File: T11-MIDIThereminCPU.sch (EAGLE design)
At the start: 66 parts, among them IC1 UA78M05DCY, IC4 QUAD_OPAMPD, IC5 4069D, J1 DCJ0202, Q1 16MHz, U1 ATMEGA328P-AU

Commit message: Add files via upload
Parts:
- removed C14: 0.1u, adafruit:C-USC0805
- removed C9: 100n, adafruit:C-USC0805
- removed IC4: QUAD_OPAMPD, adafruit:QUAD_OPAMPD
- removed JP3: (no value), adafruit:PINHD-1X12
- removed R18, R19, R20: 10k, pot:TRIM_US-B25U
- removed R21, R22, R23: 1k, resistor:R-US_R0805
- removed U$3, U$4: 1k@100MHz, adafruit:FB
- added JP4: (no value), adafruit:PINHD-1X6
- C10: value 0.1u -> 100uF; device adafruit:C-USC0805 -> adafruit:CPOL-USE3.5-8
- C7, C8: value 100n -> 100uF; device adafruit:C-USC0805 -> adafruit:CPOL-USE3.5-8
- D1, D4, D5: device diode:ZENER-DIODEDO35Z10 -> diode:1N4148DO35-7
- D2, D3: value 1N4004 -> 1N4148DO35-7; device diode:1N4004 -> diode:1N4148DO35-7
- R10, R8, R9: value 1k -> 100
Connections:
- removed net N$1: U$2G$1.4, U$4.1
- removed net N$18: IC4C.-IN, R20.S, R23.2
- removed net N$19: IC4A.-IN, R18.S, R21.1
- removed net N$21: D1.C, R23.1, U$1G$1.1
- removed net N$22: IC4B.-IN, R19.S, R22.2
- removed net N$23: D4.C, R21.2, U$6G$1.1
- removed net N$25: D5.C, R22.1, U$5G$1.1
- removed net N$3: U$2G$1.5, U$3.2
- net +12V: no longer C10.1, C14.1, IC4P.V+, JP3.1
- net +5V: no longer JP3.2
- net ANALOG_IN_1: now also D1.C, JP4.1, U$1G$1.1; no longer IC4C.OUT, JP3.5, R20.A
- net ANALOG_IN_2: now also D5.C, JP4.2, U$5G$1.1; no longer IC4B.OUT, JP3.6, R19.A
- net ANALOG_IN_3: now also D4.C, JP4.3, U$6G$1.1; no longer IC4A.OUT, JP3.7, R18.A
- net GND: now also C10.-, C7.-, C8.-, IC5B.I; no longer C10.2, C14.2, C7.1, C8.1, C9.1, IC4A.+IN, IC4B.+IN, IC4C.+IN, IC4D.+IN, IC4D.-IN, IC4P.V-, IC5F.I, JP3.3
- net INT0: now also IC5A.O; no longer IC5B.O, JP3.11
- net INT1: now also IC5F.O; no longer IC5A.O, JP3.12
- net MOSI: now also JP4.6; no longer JP3.10
- net N$10: now also C10.+; no longer C8.2
- net N$13: now also U$2G$1.5; no longer U$3.1
- net N$14: now also IC5A.I; no longer IC5B.I
- net N$2: now also U$2G$1.4; no longer U$4.2
- net N$26: now also C7.+; no longer C7.2
- net N$5: now also C8.+; no longer C9.2
- net N$6: now also IC5F.I; no longer IC5A.I
- net PC3: now also JP2.3; no longer JP2.1
- net PC5: now also JP2.1; no longer JP2.3
- net SIGNAL_OUT_1: now also JP4.4; no longer JP3.8
- net SIGNAL_OUT_2: now also JP4.5; no longer JP3.9
- net TX: no longer JP3.4
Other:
- note added: "MIDI OUTPUT"
- note added: "SENSOR CONNECTOR 1"
- note added: "SENSOR CONNECTOR 2"
- note added: "SENSOR CONNECTOR 3"
- note added: "User Select and Calibration Buttons"
- note removed: "Input buttons"
- note removed: "LED Indicators"
- note removed: "NC Op-Amp"
- note removed: "Output"
- note removed: "To Sensor Board"
- moved on the sheet: C1, C11, C12, C13, C15, C2, C3, C4, C5, C6, IC1, IC5A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

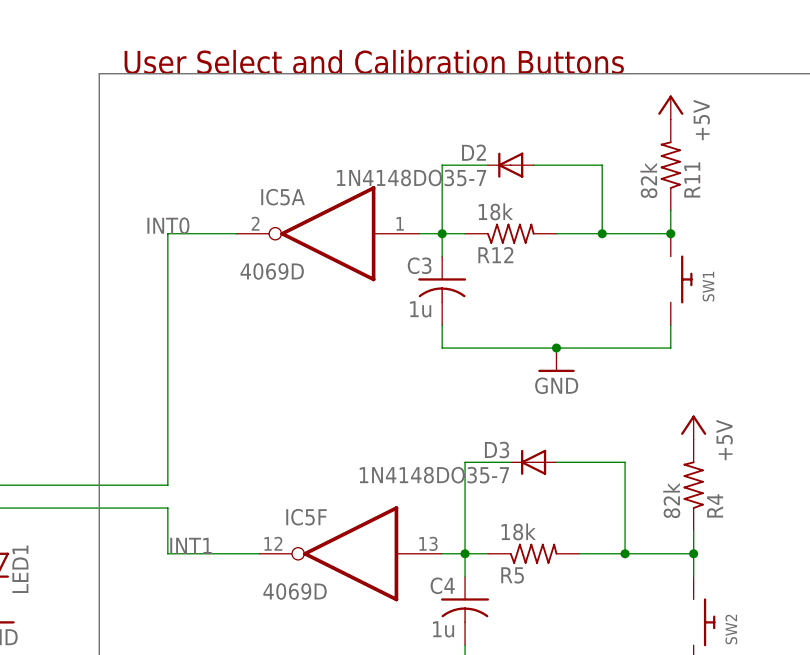
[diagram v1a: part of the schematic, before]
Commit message: Created BOM, updated parts
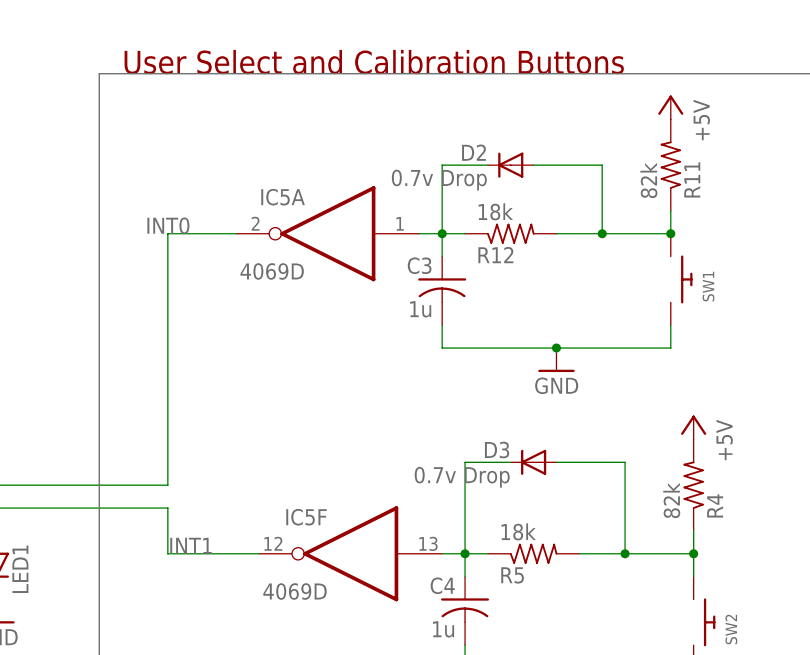
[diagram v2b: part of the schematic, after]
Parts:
- D2, D3: value 1N4148DO35-7 -> 0.7v Drop
- IC1: DIGIKEYNUMBER (none) -> 296-12290-1-ND; PARTNUMBER (none) -> UA78M05CDCYR
- IC5: DIGIKEYNUMBER (none) -> 296-28484-1-ND; PARTNUMBER (none) -> SN7414DR
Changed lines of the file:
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@@
 <?xml version="1.0" encoding="utf-8"?>
 <!DOCTYPE eagle SYSTEM "eagle.dtd">
-<eagle version="7.7.0">
+<eagle version="7.6.0">
 <drawing>
 <settings>
@@
 <setting verticaltext="up"/>
 </settings>
-<grid distance="0.05" unitdist="inch" unit="inch" style="lines" multiple="2" display="no" altdistance="0.01" altunitdist="inch" altunit="inch"/>
+<grid distance="0.1" unitdist="inch" unit="inch" style="lines" multiple="1" display="no" altdistance="0.01" altunitdist="inch" altunit="inch"/>
 <layers>
-<layer number="1" name="Top" color="4" fill="1" visible="no" active="no"/>
-<layer number="16" name="Bottom" color="1" fill="1" visible="no" active="no"/>
-<layer number="17" name="Pads" color="2" fill="1" visible="no" active="no"/>
-<layer number="18" name="Vias" color="2" fill="1" visible="no" active="no"/>
-<layer number="19" name="Unrouted" color="6" fill="1" visible="no" active="no"/>
-<layer number="20" name="Dimension" color="15" fill="1" visible="no" active="no"/>
-<layer number="21" name="tPlace" color="7" fill="1" visible="no" active="no"/>
-<layer number="22" name="bPlace" color="7" fill="1" visible="no" active="no"/>
-<layer number="23" name="tOrigins" color="15" fill="1" visible="no" active="no"/>
-<layer number="24" name="bOrigins" color="15" fill="1" visible="no" active="no"/>
-<layer number="25" name="tNames" color="7" fill="1" visible="no" active="no"/>
-<layer number="26" name="bNames" color="7" fill="1" visible="no" active="no"/>
-<layer number="27" name="tValues" color="7" fill="1" visible="no" active="no"/>
-<layer number="28" name="bValues" color="7" fill="1" visible="no" active="no"/>
+<layer number="1" name="Top" color="4" fill="1" visible="yes" active="no"/>
+<layer number="16" name="Bottom" color="1" fill="1" visible="yes" active="no"/>
+<layer number="17" name="Pads" color="2" fill="1" visible="yes" active="no"/>
+<layer number="18" name="Vias" color="2" fill="1" visible="yes" active="no"/>
+<layer number="19" name="Unrouted" color="6" fill="1" visible="yes" active="no"/>
+<layer number="20" name="Dimension" color="15" fill="1" visible="yes" active="no"/>
+<layer number="21" name="tPlace" color="7" fill="1" visible="yes" active="no"/>
+<layer number="22" name="bPlace" color="7" fill="1" visible="yes" active="no"/>
+<layer number="23" name="tOrigins" color="15" fill="1" visible="yes" active="no"/>
+<layer number="24" name="bOrigins" color="15" fill="1" visible="yes" active="no"/>
+<layer number="25" name="tNames" color="7" fill="1" visible="yes" active="no"/>
+<layer number="26" name="bNames" color="7" fill="1" visible="yes" active="no"/>
+<layer number="27" name="tValues" color="7" fill="1" visible="yes" active="no"/>
+<layer number="28" name="bValues" color="7" fill="1" visible="yes" active="no"/>
 <layer number="29" name="tStop" color="7" fill="3" visible="no" active="no"/>
 <layer number="30" name="bStop" color="7" fill="6" visible="no" active="no"/>
@@
 <layer number="35" name="tGlue" color="7" fill="4" visible="no" active="no"/>
 <layer number="36" name="bGlue" color="7" fill="5" visible="no" active="no"/>
-<layer number="37" name="tTest" color="7" fill="1" visible="no" active="no"/>
-<layer number="38" name="bTest" color="7" fill="1" visible="no" active="no"/>
+<layer number="37" name="tTest" color="7" fill="1" visible="yes" active="no"/>
+<layer number="38" name="bTest" color="7" fill="1" visible="yes" active="no"/>
 <layer number="39" name="tKeepout" color="4" fill="11" visible="no" active="no"/>
 <layer number="40" name="bKeepout" color="1" fill="11" visible="no" active="no"/>
@@
 <layer number="44" name="Drills" color="7" fill="1" visible="no" active="no"/>
 <layer number="45" name="Holes" color="7" fill="1" visible="no" active="no"/>
-<layer number="46" name="Milling" color="3" fill="1" visible="no" active="no"/>
-<layer number="47" name="Measures" color="7" fill="1" visible="no" active="no"/>
-<layer number="48" name="Document" color="7" fill="1" visible="no" active="no"/>
-<layer number="49" name="Reference" color="7" fill="1" visible="no" active="no"/>
-<layer number="50" name="dxf" color="7" fill="1" visible="no" active="no"/>
-<layer number="51" name="tDocu" color="7" fill="1" visible="no" active="no"/>
-<layer number="52" name="bDocu" color="7" fill="1" visible="no" active="no"/>
-<layer number="53" name="tGND_GNDA" color="7" fill="9" visible="no" active="no"/>
-<layer number="54" name="bGND_GNDA" color="1" fill="9" visible="no" active="no"/>
-<layer number="56" name="wert" color="7" fill="1" visible="no" active="no"/>
-<layer number="57" name="tCAD" color="7" fill="1" visible="no" active="no"/>
-<layer number="59" name="tCarbon" color="7" fill="1" visible="no" active="no"/>
-<layer number="60" name="bCarbon" color="7" fill="1" visible="no" active="no"/>
+<layer number="46" name="Milling" color="3" fill="1" visible="yes" active="no"/>
+<layer number="47" name="Measures" color="7" fill="1" visible="yes" active="no"/>
+<layer number="48" name="Document" color="7" fill="1" visible="yes" active="no"/>
+<layer number="49" name="Reference" color="7" fill="1" visible="yes" active="no"/>
+<layer number="50" name="dxf" color="7" fill="1" visible="yes" active="no"/>
+<layer number="51" name="tDocu" color="7" fill="1" visible="yes" active="no"/>
+<layer number="52" name="bDocu" color="7" fill="1" visible="yes" active="no"/>
+<layer number="53" name="tGND_GNDA" color="7" fill="9" visible="yes" active="no"/>
+<layer number="54" name="bGND_GNDA" color="1" fill="9" visible="yes" active="no"/>
+<layer number="56" name="wert" color="7" fill="1" visible="yes" active="no"/>
+<layer number="57" name="tCAD" color="7" fill="1" visible="yes" active="no"/>
+<layer number="59" name="tCarbon" color="7" fill="1" visible="yes" active="no"/>
+<layer number="60" name="bCarbon" color="7" fill="1" visible="yes" active="no"/>
 <layer number="90" name="Modules" color="5" fill="1" visible="yes" active="yes"/>
 <layer number="91" name="Nets" color="2" fill="1" visible="yes" active="yes"/>
@@
 <part name="SUPPLY1" library="supply2" deviceset="GND" device=""/>
 <part name="JP1" library="pinhead" deviceset="PINHD-2X3" device=""/>
-<part name="IC1" library="linear" deviceset="UA78M*" device="DCY" technology="05"/>
+<part name="IC1" library="linear" deviceset="UA78M*" device="DCY" technology="05">
+<attribute name="DIGIKEYNUMBER" value="296-12290-1-ND"/>
+<attribute name="PARTNUMBER" value="UA78M05CDCYR"/>
+</part>
 <part name="J1" library="con-jack" deviceset="DCJ0202" device=""/>
 <part name="C5" library="adafruit" deviceset="C-US" device="C0805" value="0.33u"/>
@@
 <part name="R12" library="resistor" deviceset="R-US_" device="R0805" value="18k"/>
 <part name="C3" library="adafruit" deviceset="C-US" device="C0805" value="1u"/>
-<part name="D2" library="diode" deviceset="1N4148" device="DO35-7"/>
+<part name="D2" library="diode" deviceset="1N4148" device="DO35-7" value="0.7v Drop"/>
 <part name="R4" library="resistor" deviceset="R-US_" device="R0805" value="82k"/>
 <part name="SW2" library="adafruit" deviceset="SWITCH_PUSHBUTTON" device="SOFTTOUCHSMD_SJ"/>
 <part name="R5" library="resistor" deviceset="R-US_" device="R0805" value="18k"/>
-<part name="D3" library="diode" deviceset="1N4148" device="DO35-7"/>
+<part name="D3" library="diode" deviceset="1N4148" device="DO35-7" value="0.7v Drop"/>
 <part name="C4" library="adafruit" deviceset="C-US" device="C0805" value="1u"/>
 <part name="U$5" library="adafruit" deviceset="MIDIJACK" device=""/>
@@
 <part name="GND25" library="supply1" deviceset="GND" device=""/>
 <part name="GND26" library="supply1" deviceset="GND" device=""/>
-<part name="IC5" library="40xx" deviceset="4069" device="D"/>
+<part name="IC5" library="40xx" deviceset="4069" device="D">
+<attribute name="DIGIKEYNUMBER" value="296-28484-1-ND"/>
+<attribute name="PARTNUMBER" value="SN7414DR"/>
+</part>
 <part name="P+5" library="supply1" deviceset="+5V" device=""/>
 <part name="GND5" library="supply1" deviceset="GND" device=""/>
@@
 <instance part="SUPPLY1" gate="GND" x="156.21" y="226.06"/>
 <instance part="JP1" gate="A" x="172.72" y="193.04"/>
-<instance part="IC1" gate="G$1" x="332.74" y="228.6"/>
+<instance part="IC1" gate="G$1" x="332.74" y="228.6">
+<attribute name="DIGIKEYNUMBER" x="332.74" y="228.6" size="1.778" layer="96" display="off"/>
+<attribute name="PARTNUMBER" x="332.74" y="228.6" size="1.778" layer="96" display="off"/>
+</instance>
 <instance part="J1" gate="G$1" x="290.83" y="223.52" rot="MR180"/>
 <instance part="C5" gate="G$1" x="320.04" y="220.98"/>
@@
 <instance part="IC5" gate="B" x="224.79" y="15.24"/>
 <instance part="IC5" gate="F" x="266.7" y="129.54" rot="MR0"/>
-<instance part="IC5" gate="A" x="264.16" y="165.1" rot="MR0"/>
+<instance part="IC5" gate="A" x="264.16" y="165.1" rot="MR0">
+<attribute name="DIGIKEYNUMBER" x="264.16" y="165.1" size="1.778" layer="96" rot="MR0" display="off"/>
+<attribute name="PARTNUMBER" x="264.16" y="165.1" size="1.778" layer="96" rot="MR0" display="off"/>
+</instance>
 <instance part="JP4" gate="A" x="100.33" y="229.87" rot="R180"/>
 <instance part="JP2" gate="A" x="195.58" y="29.21" rot="R90"/>
